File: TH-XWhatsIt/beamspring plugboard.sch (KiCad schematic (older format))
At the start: 3 parts, among them J6 BEAMSPRING PLUGBOARD COLUMNS, J7 BEAMSPRING PLUGBOARD CONNECTOR, J8 BEAMSPRING PLUGBOARD ROWS

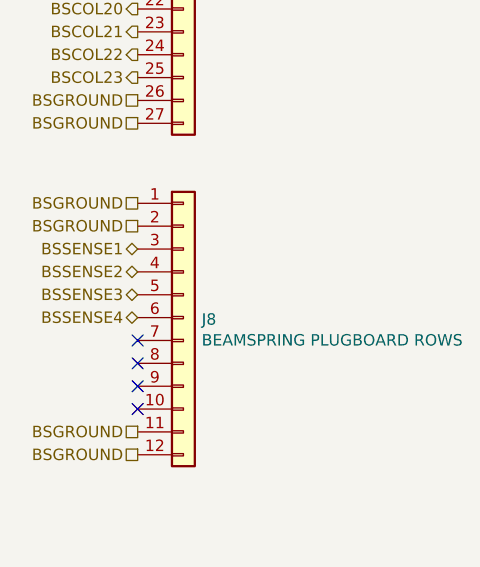
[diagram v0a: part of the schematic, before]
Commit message: version bump to 2.0 due to header position changes finished wiring up most of the plugboards, but displaywriter as per usual is the most annoying.....see changes file for more details (jan 3rd, 2020)
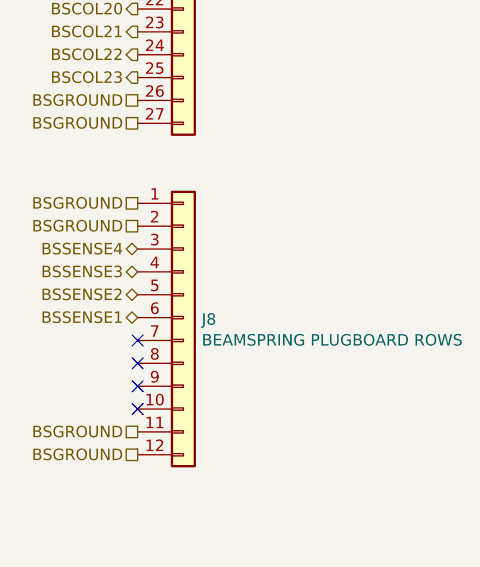
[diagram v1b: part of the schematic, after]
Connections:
- net BSSENSE1: now also J8.6 (Pin_6); no longer J8.3 (Pin_3)
- net BSSENSE2: now also J8.5 (Pin_5); no longer J8.4 (Pin_4)
- net BSSENSE3: now also J8.4 (Pin_4); no longer J8.5 (Pin_5)
- net BSSENSE4: now also J8.3 (Pin_3); no longer J8.6 (Pin_6)
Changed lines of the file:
@@
 EESchema Schematic File Version 4
+LIBS:TH-XWhatsIt-cache
 EELAYER 30 0
 EELAYER END
@@
 NoConn ~ 2700 4850
 NoConn ~ 2700 4750
+Text HLabel 2700 4650 0    50   BiDi ~ 0
+BSSENSE1
+Text HLabel 2700 4550 0    50   BiDi ~ 0
+BSSENSE2
+Text HLabel 2700 4450 0    50   BiDi ~ 0
+BSSENSE3
 Text HLabel 2700 4350 0    50   BiDi ~ 0
-BSSENSE1
-Text HLabel 2700 4450 0    50   BiDi ~ 0
-BSSENSE2
-Text HLabel 2700 4550 0    50   BiDi ~ 0
-BSSENSE3
-Text HLabel 2700 4650 0    50   BiDi ~ 0
 BSSENSE4
 Text HLabel 5000 3800 0    50   BiDi ~ 0

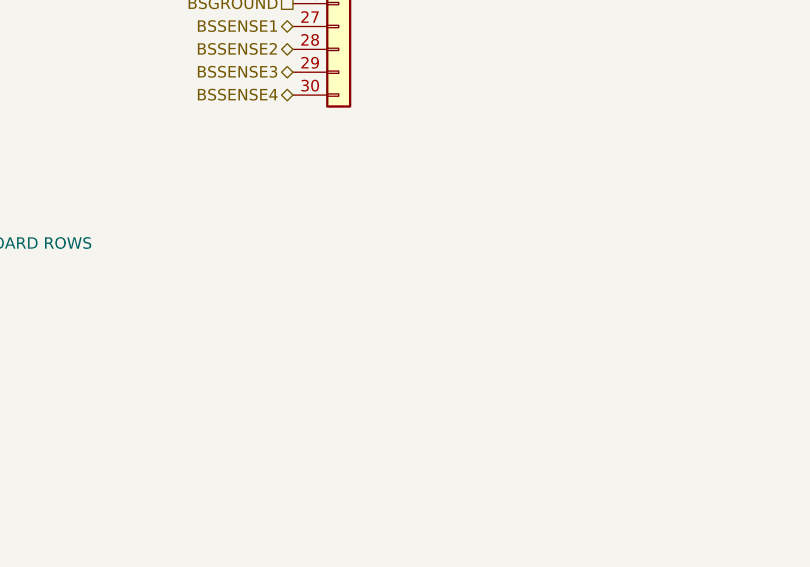
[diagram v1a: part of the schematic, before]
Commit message: finished wiring the dispalywriter plugboard, and added grounding straps to plugboards
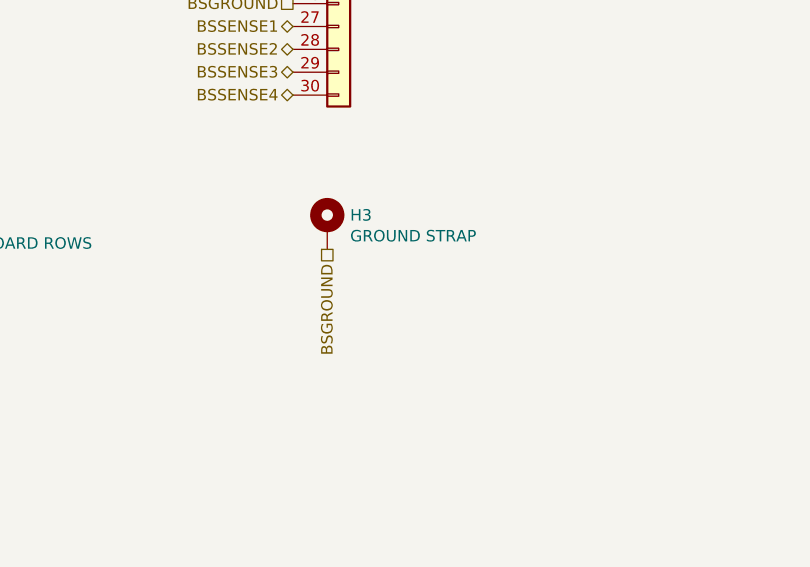
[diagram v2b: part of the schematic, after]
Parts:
- added H3: GROUND STRAP, MountingHole:MountingHole_2.2mm_M2_Pad_Via, symbol Mechanical:MountingHole_Pad
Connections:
- net BSGROUND: now also H3.1
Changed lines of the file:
@@
 Text Notes 3950 7750 0    50   ~ 0
 Copyright Rainy Day Plans.\nThis documentation describes Open Hardware and is licensed under the\nCERN OHL v. 1.2.\nYou may redistribute and modify this documentation under the terms of the\nCERN OHL v.1.2. (http://ohwr.org/cernohl). This documentation is distributed\nWITHOUT ANY EXPRESS OR IMPLIED WARRANTY, INCLUDING OF\nMERCHANTABILITY, SATISFACTORY QUALITY AND FITNESS FOR A\nPARTICULAR PURPOSE. Please see the CERN OHL v.1.2 for applicable\nconditions
+$Comp
+L Mechanical:MountingHole_Pad H3
+U 1 1 5E3A02A4
+P 5150 4675
+F 0 "H3" H 5250 4724 50  0000 L CNN
+F 1 "GROUND STRAP" H 5250 4633 50  0000 L CNN
+F 2 "MountingHole:MountingHole_2.2mm_M2_Pad_Via" H 5150 4675 50  0001 C CNN
+F 3 "~" H 5150 4675 50  0001 C CNN
+	1    5150 4675
+	1    0    0    -1
+$EndComp
+Text HLabel 5150 4775 3    50   UnSpc ~ 0
+BSGROUND
 $EndSCHEMATC

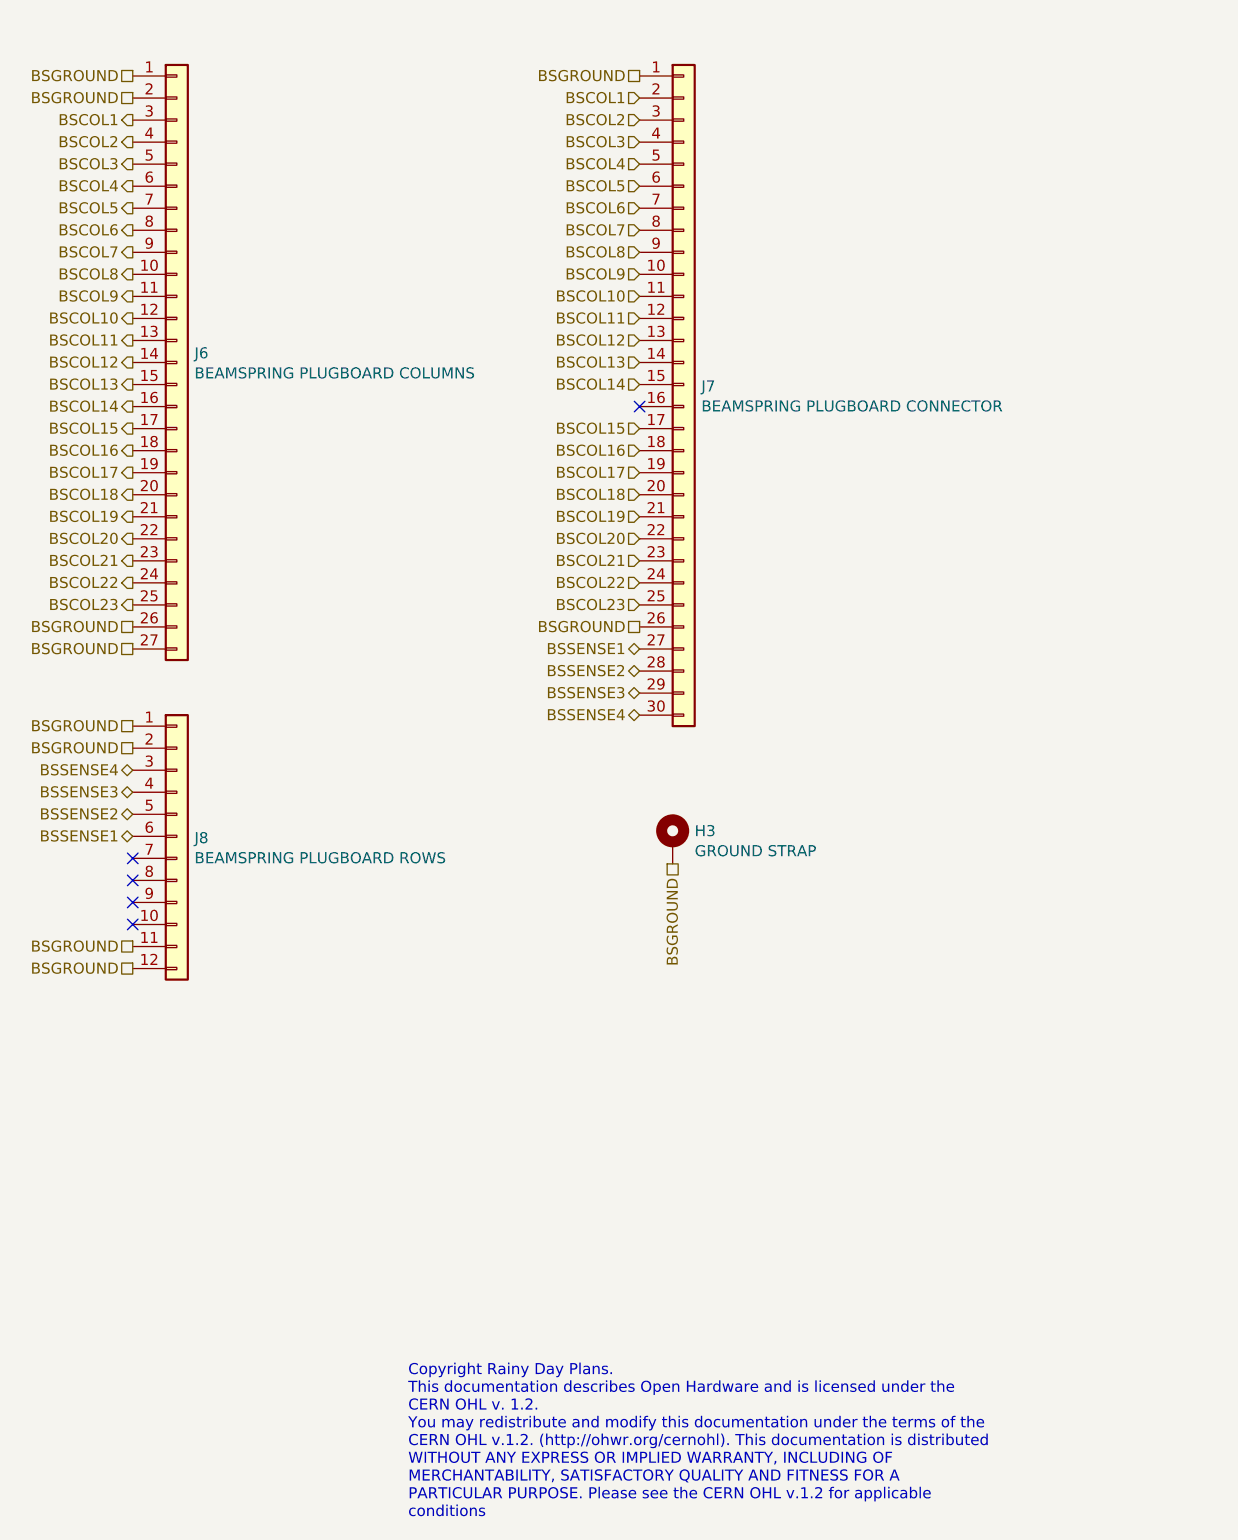
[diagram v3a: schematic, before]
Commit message: initial update to switch to smd, so now th prefix is a misnomer
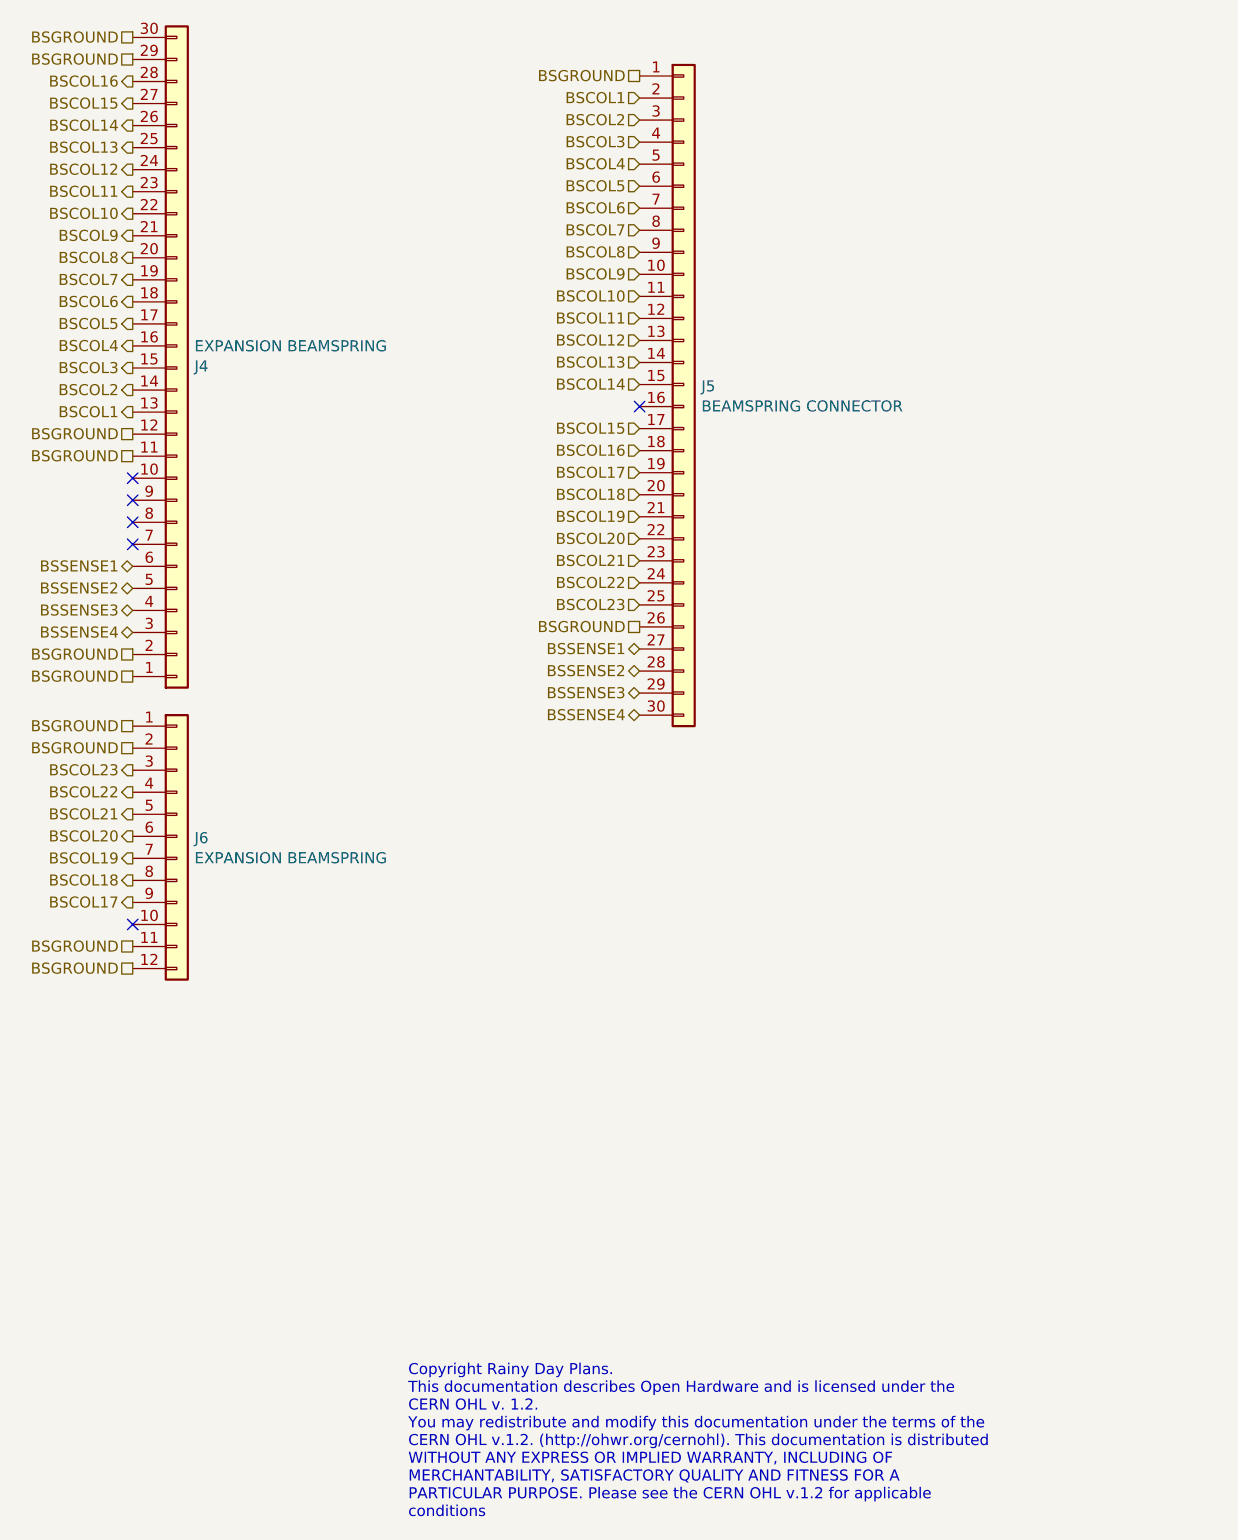
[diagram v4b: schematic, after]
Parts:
- removed H3: GROUND STRAP, MountingHole:MountingHole_2.2mm_M2_Pad_Via, symbol Mechanical:MountingHole_Pad
- removed J6: BEAMSPRING PLUGBOARD COLUMNS, Connector_PinSocket_2.54mm:PinSocket_1x27_P2.54mm_Vertical, symbol Connector_Generic:Conn_01x27
- removed J7: BEAMSPRING PLUGBOARD CONNECTOR, TH-XWhatsIt:3..6mm_cardedge, symbol Connector_Generic:Conn_01x30
- added J4: EXPANSION BEAMSPRING, TH-XWhatsIt:30-pin-castelated-connector, symbol Connector_Generic:Conn_01x30
- added J5: BEAMSPRING CONNECTOR, TH-XWhatsIt:30-pin-universal-beamspring-connector, symbol Connector_Generic:Conn_01x30
- J6: renamed from J8; value BEAMSPRING PLUGBOARD ROWS -> EXPANSION BEAMSPRING; footprint Connector_PinSocket_2.54mm:PinSocket_1x12_P2.54mm_Vertical -> TH-XWhatsIt:12-pin-castelated-connector
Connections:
- net BSCOL1: now also J4.13 (Pin_13), J5.2 (Pin_2)
- net BSCOL10: now also J4.22 (Pin_22), J5.11 (Pin_11)
- net BSCOL11: now also J4.23 (Pin_23), J5.12 (Pin_12)
- net BSCOL12: now also J4.24 (Pin_24), J5.13 (Pin_13)
- net BSCOL13: now also J4.25 (Pin_25), J5.14 (Pin_14)
- net BSCOL14: now also J4.26 (Pin_26), J5.15 (Pin_15)
- net BSCOL15: now also J4.27 (Pin_27), J5.17 (Pin_17)
- net BSCOL16: now also J4.28 (Pin_28), J5.18 (Pin_18)
- net BSCOL17: now also J6.9 (Pin_9), J5.19 (Pin_19)
- net BSCOL18: now also J6.8 (Pin_8), J5.20 (Pin_20)
- net BSCOL19: now also J6.7 (Pin_7), J5.21 (Pin_21)
- net BSCOL2: now also J4.14 (Pin_14), J5.3 (Pin_3)
- net BSCOL20: now also J6.6 (Pin_6), J5.22 (Pin_22)
- net BSCOL21: now also J6.5 (Pin_5), J5.23 (Pin_23)
- net BSCOL22: now also J6.4 (Pin_4), J5.24 (Pin_24)
- net BSCOL23: now also J6.3 (Pin_3), J5.25 (Pin_25)
- net BSCOL3: now also J4.15 (Pin_15), J5.4 (Pin_4)
- net BSCOL4: now also J4.16 (Pin_16), J5.5 (Pin_5)
- net BSCOL5: now also J4.17 (Pin_17), J5.6 (Pin_6)
- net BSCOL6: now also J4.18 (Pin_18), J5.7 (Pin_7)
- net BSCOL7: now also J4.19 (Pin_19), J5.8 (Pin_8)
- net BSCOL8: now also J4.20 (Pin_20), J5.9 (Pin_9)
- net BSCOL9: now also J4.21 (Pin_21), J5.10 (Pin_10)
- net BSGROUND: now also J4.1 (Pin_1), J4.11 (Pin_11), J4.12 (Pin_12), J4.2 (Pin_2), J4.29 (Pin_29), J4.30 (Pin_30), J5.1 (Pin_1), J5.26 (Pin_26)
- net BSSENSE1: now also J4.6 (Pin_6), J5.27 (Pin_27); no longer J6.6 (Pin_6)
- net BSSENSE2: now also J4.5 (Pin_5), J5.28 (Pin_28); no longer J6.5 (Pin_5)
- net BSSENSE3: now also J4.4 (Pin_4), J5.29 (Pin_29); no longer J6.4 (Pin_4)
- net BSSENSE4: now also J4.3 (Pin_3), J5.30 (Pin_30); no longer J6.3 (Pin_3)
- no-connect marks 5 -> 6
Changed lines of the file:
@@
 $Descr A4 11693 8268
 encoding utf-8
-Sheet 3 4
+Sheet 2 3
 Title "Beamspring plugboard to convert controller signals"
 Date "2020-01-31"
@@
 $EndDescr
 $Comp
-L Connector_Generic:Conn_01x27 J?
-U 1 1 5E982560
-P 2900 2500
-AR Path="/5E982560" Ref="J?"  Part="1"
-AR Path="/5E9772A5/5E982560" Ref="J6"  Part="1"
-F 0 "J6" H 2980 2542 50  0000 L CNN
-F 1 "BEAMSPRING PLUGBOARD COLUMNS" H 2980 2451 50  0000 L CNN
-F 2 "Connector_PinSocket_2.54mm:PinSocket_1x27_P2.54mm_Vertical" H 2900 2500 50  0001 C CNN
-F 3 "~" H 2900 2500 50  0001 C CNN
-	1    2900 2500
-	1    0    0    -1
-$EndComp
-$Comp
 L Connector_Generic:Conn_01x12 J?
 U 1 1 5E98257D
 P 2900 4650
 AR Path="/5E98257D" Ref="J?"  Part="1"
-AR Path="/5E9772A5/5E98257D" Ref="J8"  Part="1"
-F 0 "J8" H 2980 4642 50  0000 L CNN
-F 1 "BEAMSPRING PLUGBOARD ROWS" H 2980 4551 50  0000 L CNN
-F 2 "Connector_PinSocket_2.54mm:PinSocket_1x12_P2.54mm_Vertical" H 2900 4650 50  0001 C CNN
+AR Path="/5E9772A5/5E98257D" Ref="J6"  Part="1"
+F 0 "J6" H 2980 4642 50  0000 L CNN
+F 1 "EXPANSION BEAMSPRING" H 2980 4551 50  0000 L CNN
+F 2 "TH-XWhatsIt:12-pin-castelated-connector" H 2900 4650 50  0001 C CNN
 F 3 "~" H 2900 4650 50  0001 C CNN
 	1    2900 4650
 	1    0    0    -1
 $EndComp
-$Comp
-L Connector_Generic:Conn_01x30 J7
-U 1 1 5E9AB53F
-P 5200 2600
-F 0 "J7" H 5280 2592 50  0000 L CNN
-F 1 "BEAMSPRING PLUGBOARD CONNECTOR" H 5280 2501 50  0000 L CNN
-F 2 "TH-XWhatsIt:3..6mm_cardedge" H 5200 2600 50  0001 C CNN
-F 3 "~" H 5200 2600 50  0001 C CNN
-	1    5200 2600
-	1    0    0    -1
-$EndComp
 NoConn ~ 5000 2700
-Text HLabel 2700 1400 0    50   Output ~ 0
+Text HLabel 2700 2725 0    50   Output ~ 0
 BSCOL1
-Text HLabel 2700 1500 0    50   Output ~ 0
+Text HLabel 2700 2625 0    50   Output ~ 0
 BSCOL2
-Text HLabel 2700 1600 0    50   Output ~ 0
+Text HLabel 2700 2525 0    50   Output ~ 0
 BSCOL3
-Text HLabel 2700 1700 0    50   Output ~ 0
+Text HLabel 2700 2425 0    50   Output ~ 0
 BSCOL4
-Text HLabel 2700 1800 0    50   Output ~ 0
+Text HLabel 2700 2325 0    50   Output ~ 0
 BSCOL5
-Text HLabel 2700 1900 0    50   Output ~ 0
+Text HLabel 2700 2225 0    50   Output ~ 0
 BSCOL6
-Text HLabel 2700 2000 0    50   Output ~ 0
+Text HLabel 2700 2125 0    50   Output ~ 0
 BSCOL7
-Text HLabel 2700 2100 0    50   Output ~ 0
+Text HLabel 2700 2025 0    50   Output ~ 0
 BSCOL8
-Text HLabel 2700 2200 0    50   Output ~ 0
+Text HLabel 2700 1925 0    50   Output ~ 0
 BSCOL9
-Text HLabel 2700 2300 0    50   Output ~ 0
+Text HLabel 2700 1825 0    50   Output ~ 0
 BSCOL10
-Text HLabel 2700 2400 0    50   Output ~ 0
+Text HLabel 2700 1725 0    50   Output ~ 0
 BSCOL11
-Text HLabel 2700 2500 0    50   Output ~ 0
+Text HLabel 2700 1625 0    50   Output ~ 0
 BSCOL12
-Text HLabel 2700 2600 0    50   Output ~ 0
+Text HLabel 2700 1525 0    50   Output ~ 0
 BSCOL13
-Text HLabel 2700 2700 0    50   Output ~ 0
+Text HLabel 2700 1425 0    50   Output ~ 0
 BSCOL14
-Text HLabel 2700 2800 0    50   Output ~ 0
+Text HLabel 2700 1325 0    50   Output ~ 0
 BSCOL15
-Text HLabel 2700 2900 0    50   Output ~ 0
+Text HLabel 2700 1225 0    50   Output ~ 0
 BSCOL16
-Text HLabel 2700 3000 0    50   Output ~ 0
+Text HLabel 2700 4950 0    50   Output ~ 0
 BSCOL17
-Text HLabel 2700 3100 0    50   Output ~ 0
+Text HLabel 2700 4850 0    50   Output ~ 0
 BSCOL18
-Text HLabel 2700 3200 0    50   Output ~ 0
+Text HLabel 2700 4750 0    50   Output ~ 0
 BSCOL19
-Text HLabel 2700 3300 0    50   Output ~ 0
+Text HLabel 2700 4650 0    50   Output ~ 0
 BSCOL20
-Text HLabel 2700 3400 0    50   Output ~ 0
+Text HLabel 2700 4550 0    50   Output ~ 0
 BSCOL21
-Text HLabel 2700 3500 0    50   Output ~ 0
+Text HLabel 2700 4450 0    50   Output ~ 0
 BSCOL22
-Text HLabel 2700 3600 0    50   Output ~ 0
+Text HLabel 2700 4350 0    50   Output ~ 0
 BSCOL23
 Text HLabel 5000 1300 0    50   Input ~ 0
@@
 Text HLabel 5000 3600 0    50   Input ~ 0
 BSCOL23
-NoConn ~ 2700 5050
-NoConn ~ 2700 4950
-NoConn ~ 2700 4850
-NoConn ~ 2700 4750
-Text HLabel 2700 4650 0    50   BiDi ~ 0
+Text HLabel 2700 3425 0    50   BiDi ~ 0
 BSSENSE1
-Text HLabel 2700 4550 0    50   BiDi ~ 0
+Text HLabel 2700 3525 0    50   BiDi ~ 0
 BSSENSE2
-Text HLabel 2700 4450 0    50   BiDi ~ 0
+Text HLabel 2700 3625 0    50   BiDi ~ 0
 BSSENSE3
-Text HLabel 2700 4350 0    50   BiDi ~ 0
+Text HLabel 2700 3725 0    50   BiDi ~ 0
 BSSENSE4
 Text HLabel 5000 3800 0    50   BiDi ~ 0
@@
 Text HLabel 5000 4100 0    50   BiDi ~ 0
 BSSENSE4
-Text HLabel 2700 1200 0    50   UnSpc ~ 0
+Text HLabel 2700 1025 0    50   UnSpc ~ 0
 BSGROUND
-Text HLabel 2700 1300 0    50   UnSpc ~ 0
+Text HLabel 2700 1125 0    50   UnSpc ~ 0
 BSGROUND
-Text HLabel 2700 3700 0    50   UnSpc ~ 0
+Text HLabel 2700 3825 0    50   UnSpc ~ 0
 BSGROUND
-Text HLabel 2700 3800 0    50   UnSpc ~ 0
+Text HLabel 2700 3925 0    50   UnSpc ~ 0
 BSGROUND
 Text HLabel 2700 4150 0    50   UnSpc ~ 0
@@
 Text Notes 3950 7750 0    50   ~ 0
 Copyright Rainy Day Plans.\nThis documentation describes Open Hardware and is licensed under the\nCERN OHL v. 1.2.\nYou may redistribute and modify this documentation under the terms of the\nCERN OHL v.1.2. (http://ohwr.org/cernohl). This documentation is distributed\nWITHOUT ANY EXPRESS OR IMPLIED WARRANTY, INCLUDING OF\nMERCHANTABILITY, SATISFACTORY QUALITY AND FITNESS FOR A\nPARTICULAR PURPOSE. Please see the CERN OHL v.1.2 for applicable\nconditions
+NoConn ~ 2700 5050
+Text HLabel 2700 2825 0    50   UnSpc ~ 0
+BSGROUND
+Text HLabel 2700 2925 0    50   UnSpc ~ 0
+BSGROUND
 $Comp
-L Mechanical:MountingHole_Pad H3
-U 1 1 5E3A02A4
-P 5150 4675
-F 0 "H3" H 5250 4724 50  0000 L CNN
-F 1 "GROUND STRAP" H 5250 4633 50  0000 L CNN
-F 2 "MountingHole:MountingHole_2.2mm_M2_Pad_Via" H 5150 4675 50  0001 C CNN
-F 3 "~" H 5150 4675 50  0001 C CNN
-	1    5150 4675
+L Connector_Generic:Conn_01x30 J?
+U 1 1 5F5BC1B2
+P 2900 2525
+AR Path="/5F5BC1B2" Ref="J?"  Part="1"
+AR Path="/5E9772A5/5F5BC1B2" Ref="J4"  Part="1"
+F 0 "J4" H 2980 2517 50  0000 L CNN
+F 1 "EXPANSION BEAMSPRING" H 2980 2426 50  0000 L CNN
+F 2 "TH-XWhatsIt:30-pin-castelated-connector" H 2900 2525 50  0001 C CNN
+F 3 "~" H 2900 2525 50  0001 C CNN
+	1    2900 2525
+	1    0    0    1
+$EndComp
+$Comp
+L Connector_Generic:Conn_01x30 J?
+U 1 1 5F5D0CF1
+P 5200 2600
+AR Path="/5F5D0CF1" Ref="J?"  Part="1"
+AR Path="/5E9772A5/5F5D0CF1" Ref="J5"  Part="1"
+F 0 "J5" H 5280 2592 50  0000 L CNN
+F 1 "BEAMSPRING CONNECTOR" H 5280 2501 50  0000 L CNN
+F 2 "TH-XWhatsIt:30-pin-universal-beamspring-connector" H 5200 2600 50  0001 C CNN
+F 3 "~" H 5200 2600 50  0001 C CNN
+	1    5200 2600
 	1    0    0    -1
 $EndComp
-Text HLabel 5150 4775 3    50   UnSpc ~ 0
-BSGROUND
+NoConn ~ 2700 3025
+NoConn ~ 2700 3125
+NoConn ~ 2700 3225
+NoConn ~ 2700 3325
 $EndSCHEMATC
